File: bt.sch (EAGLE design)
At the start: 16 parts, among them IC1 BLUETOOTH-RN42 HID, Q1 MOSFET-NCHANNELSMD, Q2 MOSFET-NCHANNELSMD

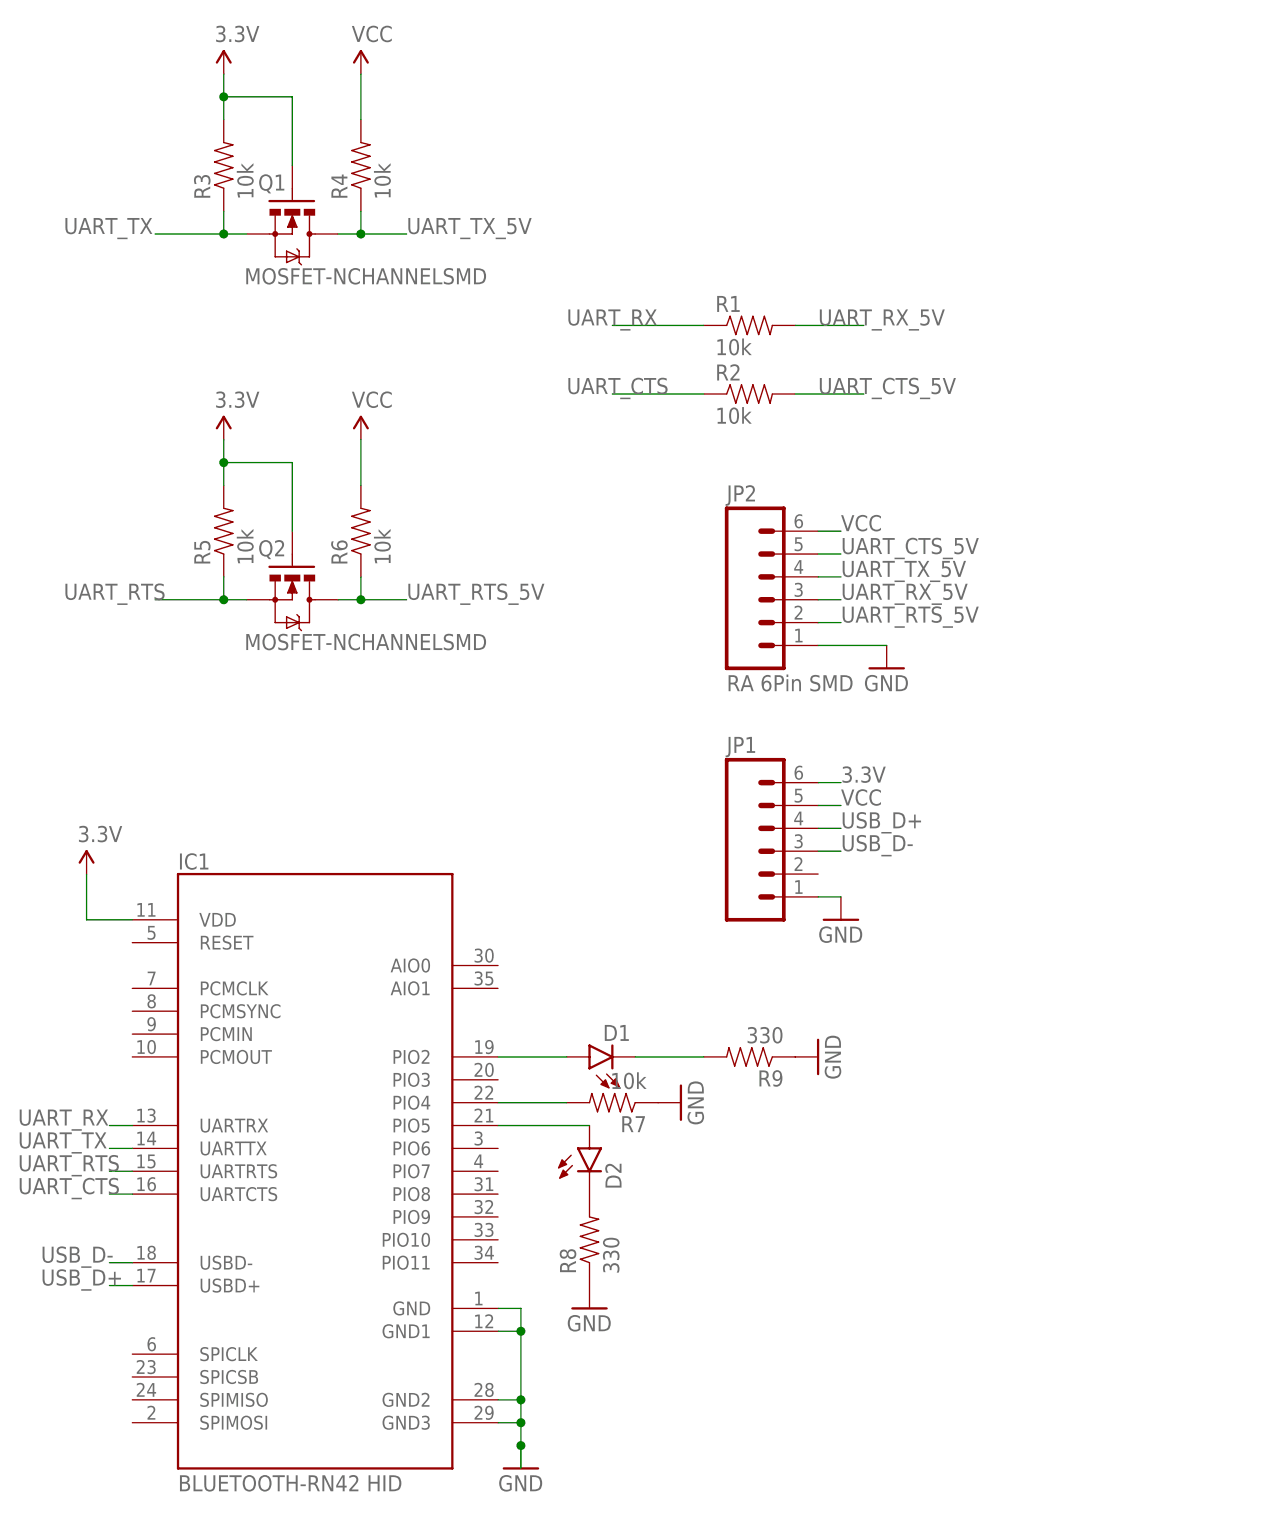
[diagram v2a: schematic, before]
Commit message: Removed silk from bt module and renamed headers
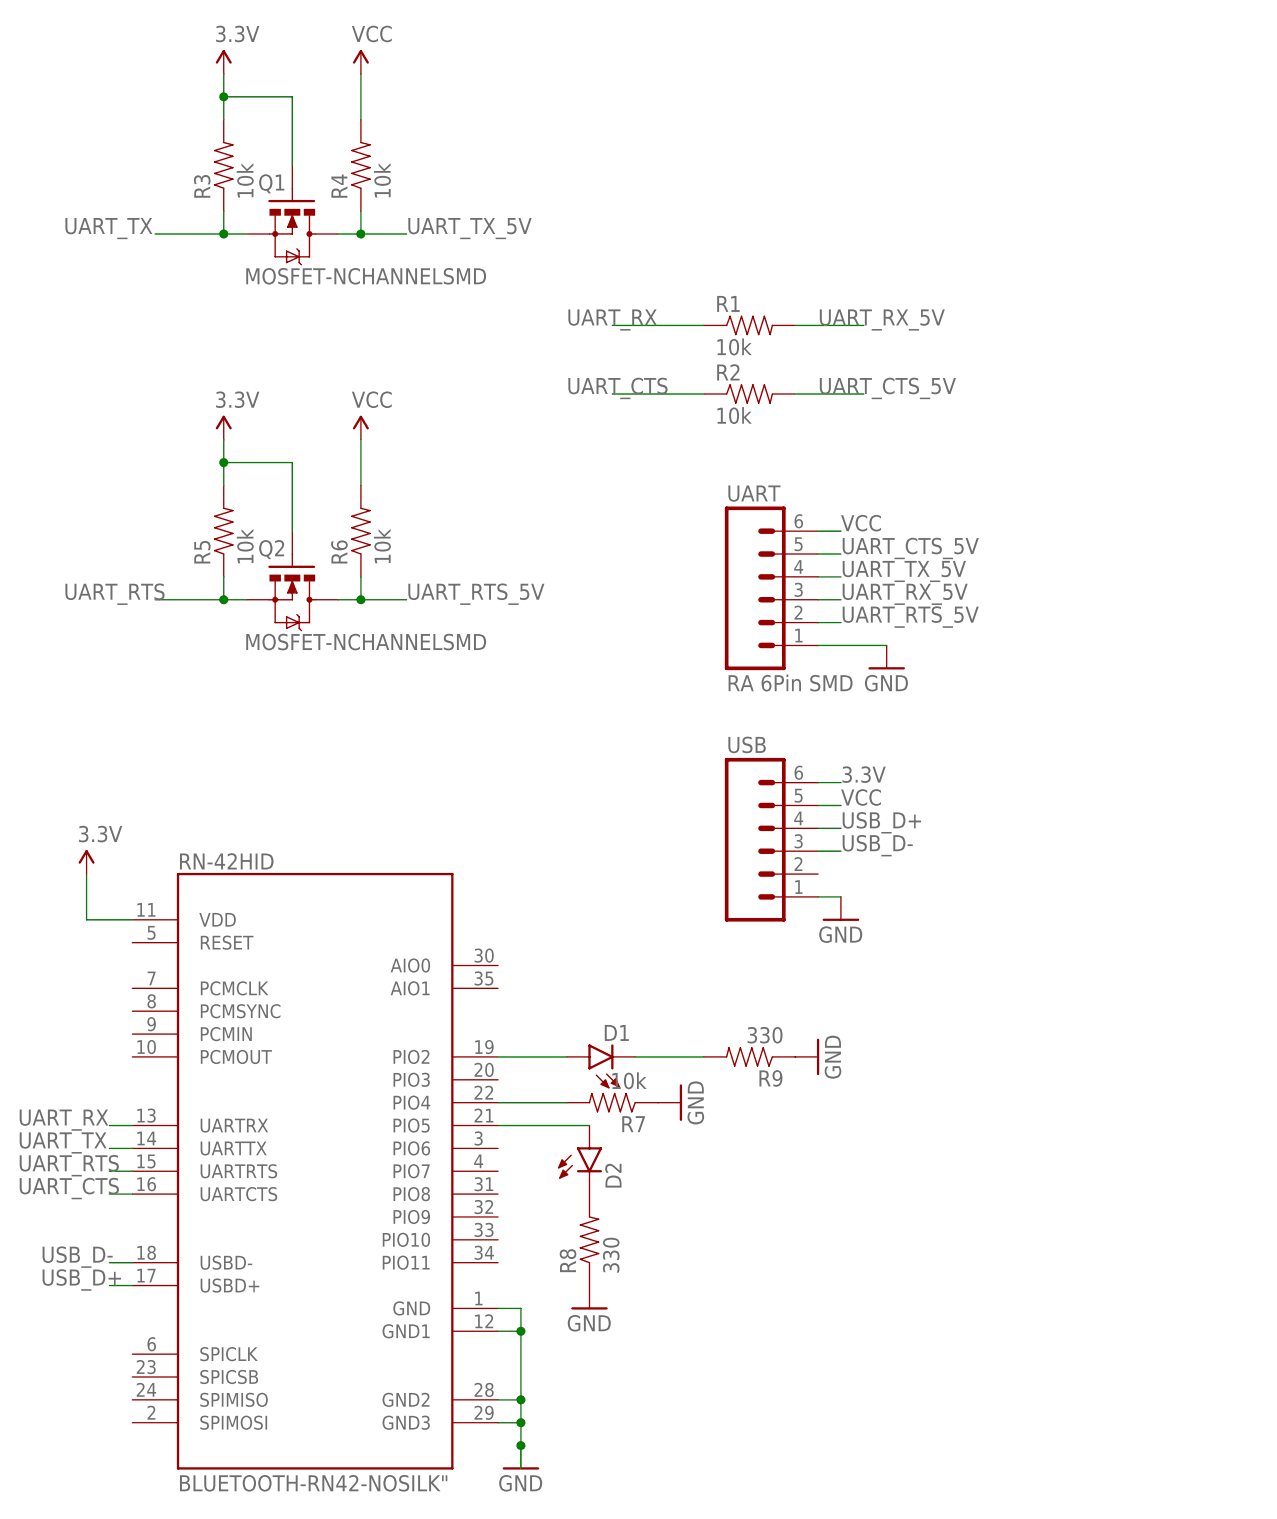
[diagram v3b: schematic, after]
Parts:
- removed IC1: BLUETOOTH-RN42 HID, SparkFun-RF:BLUETOOTH-RN41"
- added RN-42HID: BLUETOOTH-RN42-NOSILK", mine:BLUETOOTH-RN42-NOSILK"
- renumbered JP1 to USB, JP2 to UART
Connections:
- net GND: now also RN-42HID.GND, RN-42HID.GND1, RN-42HID.GND2, RN-42HID.GND3; no longer IC1.GND, IC1.GND1, IC1.GND2, IC1.GND3
- net N$10: now also RN-42HID.PIO5; no longer IC1.PIO5
- net N$8: now also RN-42HID.PIO2; no longer IC1.PIO2
- net N$9: now also RN-42HID.PIO4; no longer IC1.PIO4
- net UART_CTS: now also RN-42HID.UARTCTS; no longer IC1.UARTCTS
- net UART_RTS: now also RN-42HID.UARTRTS; no longer IC1.UARTRTS
- net UART_RX: now also RN-42HID.UARTRX; no longer IC1.UARTRX
- net UART_TX: now also RN-42HID.UARTTX; no longer IC1.UARTTX
- net USB_D+: now also RN-42HID.USBD+; no longer IC1.USBD+
- net USB_D-: now also RN-42HID.USBD-; no longer IC1.USBD-
- net VCC: now also RN-42HID.VDD; no longer IC1.VDD
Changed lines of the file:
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@@
 </classes>
 <parts>
-<part name="IC1" library="SparkFun-RF" deviceset="BLUETOOTH-RN41" device="&quot;" value="BLUETOOTH-RN42 HID"/>
 <part name="Q2" library="SparkFun" deviceset="MOSFET-NCHANNEL" device="SMD"/>
 <part name="P+7" library="SparkFun" deviceset="VCC" device="" value="3.3V"/>
@@
 <part name="GND5" library="SparkFun" deviceset="GND" device=""/>
 <part name="GND6" library="SparkFun" deviceset="GND" device=""/>
-<part name="JP2" library="mine" deviceset="M06" device="SMD-NOHOLES" value="RA 6Pin SMD"/>
-<part name="JP1" library="mine" deviceset="M06" device="SMD-FEMALE-V2-NOSILK"/>
+<part name="UART" library="mine" deviceset="M06" device="SMD-NOHOLES" value="RA 6Pin SMD"/>
+<part name="USB" library="mine" deviceset="M06" device="SMD-FEMALE-V2-NOSILK"/>
+<part name="RN-42HID" library="mine" deviceset="BLUETOOTH-RN42-NOSILK" device="&quot;"/>
 </parts>
 <sheets>
@@
 </plain>
 <instances>
-<instance part="IC1" gate="G$1" x="27.94" y="35.56"/>
 <instance part="Q2" gate="G$1" x="25.4" y="99.06" smashed="yes" rot="R270">
 <attribute name="NAME" x="21.59" y="103.886" size="1.778" layer="95"/>
@@
 <instance part="GND5" gate="1" x="83.82" y="48.26" rot="R90"/>
 <instance part="GND6" gate="1" x="58.42" y="20.32"/>
-<instance part="JP2" gate="G$1" x="78.74" y="99.06"/>
-<instance part="JP1" gate="G$1" x="78.74" y="71.12"/>
+<instance part="UART" gate="G$1" x="78.74" y="99.06"/>
+<instance part="USB" gate="G$1" x="78.74" y="71.12"/>
+<instance part="RN-42HID" gate="G$1" x="27.94" y="35.56"/>
 </instances>
 <busses>
@@
 </segment>
 <segment>
-<pinref part="IC1" gate="G$1" pin="UARTTX"/>
 <wire x1="7.62" y1="38.1" x2="5.08" y2="38.1" width="0.1524" layer="91"/>
 <label x="-5.08" y="38.1" size="1.778" layer="95"/>
+<pinref part="RN-42HID" gate="G$1" pin="UARTTX"/>
 </segment>
 </net>
@@
 <wire x1="83.82" y1="78.74" x2="86.36" y2="78.74" width="0.1524" layer="91"/>
 <label x="86.36" y="78.74" size="1.778" layer="95"/>
-<pinref part="JP1" gate="G$1" pin="6"/>
+<pinref part="USB" gate="G$1" pin="6"/>
 </segment>
 </net>
@@
 <wire x1="83.82" y1="101.6" x2="86.36" y2="101.6" width="0.1524" layer="91"/>
 <label x="86.36" y="101.6" size="1.778" layer="95"/>
-<pinref part="JP2" gate="G$1" pin="4"/>
+<pinref part="UART" gate="G$1" pin="4"/>
 </segment>
 </net>
@@
 </segment>
 <segment>
-<pinref part="IC1" gate="G$1" pin="UARTRX"/>
 <wire x1="7.62" y1="40.64" x2="5.08" y2="40.64" width="0.1524" layer="91"/>
 <label x="-5.08" y="40.64" size="1.778" layer="95"/>
+<pinref part="RN-42HID" gate="G$1" pin="UARTRX"/>
 </segment>
 </net>
@@
 <wire x1="83.82" y1="99.06" x2="86.36" y2="99.06" width="0.1524" layer="91"/>
 <label x="86.36" y="99.06" size="1.778" layer="95"/>
-<pinref part="JP2" gate="G$1" pin="3"/>
+<pinref part="UART" gate="G$1" pin="3"/>
 </segment>
 </net>
@@
 </segment>
 <segment>
-<pinref part="IC1" gate="G$1" pin="VDD"/>
 <wire x1="7.62" y1="63.5" x2="2.54" y2="63.5" width="0.1524" layer="91"/>
 <wire x1="2.54" y1="63.5" x2="2.54" y2="68.58" width="0.1524" layer="91"/>
 <pinref part="P+2" gate="1" pin="VCC"/>
+<pinref part="RN-42HID" gate="G$1" pin="VDD"/>
 </segment>
 <segment>
 <wire x1="83.82" y1="76.2" x2="86.36" y2="76.2" width="0.1524" layer="91"/>
 <label x="86.36" y="76.2" size="1.778" layer="95"/>
-<pinref part="JP1" gate="G$1" pin="5"/>
+<pinref part="USB" gate="G$1" pin="5"/>
 </segment>
 <segment>
 <wire x1="83.82" y1="106.68" x2="86.36" y2="106.68" width="0.1524" layer="91"/>
 <label x="86.36" y="106.68" size="1.778" layer="95"/>
-<pinref part="JP2" gate="G$1" pin="6"/>
+<pinref part="UART" gate="G$1" pin="6"/>
 </segment>
 </net>
@@
 </segment>
 <segment>
-<pinref part="IC1" gate="G$1" pin="UARTRTS"/>
 <wire x1="7.62" y1="35.56" x2="5.08" y2="35.56" width="0.1524" layer="91"/>
 <label x="-5.08" y="35.56" size="1.778" layer="95"/>
+<pinref part="RN-42HID" gate="G$1" pin="UARTRTS"/>
 </segment>
 </net>
@@
 <wire x1="83.82" y1="96.52" x2="86.36" y2="96.52" width="0.1524" layer="91"/>
 <label x="86.36" y="96.52" size="1.778" layer="95"/>
-<pinref part="JP2" gate="G$1" pin="2"/>
+<pinref part="UART" gate="G$1" pin="2"/>
 </segment>
 </net>
@@
 </segment>
 <segment>
-<pinref part="IC1" gate="G$1" pin="UARTCTS"/>
 <wire x1="7.62" y1="33.02" x2="5.08" y2="33.02" width="0.1524" layer="91"/>
 <label x="-5.08" y="33.02" size="1.778" layer="95"/>
+<pinref part="RN-42HID" gate="G$1" pin="UARTCTS"/>
 </segment>
 </net>
@@
 <wire x1="83.82" y1="104.14" x2="86.36" y2="104.14" width="0.1524" layer="91"/>
 <label x="86.36" y="104.14" size="1.778" layer="95"/>
-<pinref part="JP2" gate="G$1" pin="5"/>
+<pinref part="UART" gate="G$1" pin="5"/>
 </segment>
 </net>
 <net name="USB_D-" class="0">
 <segment>
-<pinref part="IC1" gate="G$1" pin="USBD-"/>
 <wire x1="7.62" y1="25.4" x2="5.08" y2="25.4" width="0.1524" layer="91"/>
 <label x="-2.54" y="25.4" size="1.778" layer="95"/>
+<pinref part="RN-42HID" gate="G$1" pin="USBD-"/>
 </segment>
 <segment>
 <wire x1="83.82" y1="71.12" x2="86.36" y2="71.12" width="0.1524" layer="91"/>
 <label x="86.36" y="71.12" size="1.778" layer="95"/>
-<pinref part="JP1" gate="G$1" pin="3"/>
+<pinref part="USB" gate="G$1" pin="3"/>
 </segment>
 </net>
 <net name="USB_D+" class="0">
 <segment>
-<pinref part="IC1" gate="G$1" pin="USBD+"/>
 <wire x1="7.62" y1="22.86" x2="5.08" y2="22.86" width="0.1524" layer="91"/>
 <label x="-2.54" y="22.86" size="1.778" layer="95"/>
+<pinref part="RN-42HID" gate="G$1" pin="USBD+"/>
 </segment>
 <segment>
 <wire x1="83.82" y1="73.66" x2="86.36" y2="73.66" width="0.1524" layer="91"/>
 <label x="86.36" y="73.66" size="1.778" layer="95"/>
-<pinref part="JP1" gate="G$1" pin="4"/>
+<pinref part="USB" gate="G$1" pin="4"/>
 </segment>
 </net>
 <net name="N$8" class="0">
 <segment>
-<pinref part="IC1" gate="G$1" pin="PIO2"/>
 <wire x1="48.26" y1="48.26" x2="55.88" y2="48.26" width="0.1524" layer="91"/>
 <pinref part="D1" gate="G$1" pin="A"/>
+<pinref part="RN-42HID" gate="G$1" pin="PIO2"/>
 </segment>
 </net>
 <net name="N$9" class="0">
 <segment>
-<pinref part="IC1" gate="G$1" pin="PIO4"/>
 <wire x1="48.26" y1="43.18" x2="55.88" y2="43.18" width="0.1524" layer="91"/>
 <pinref part="R7" gate="G$1" pin="2"/>
+<pinref part="RN-42HID" gate="G$1" pin="PIO4"/>
 </segment>
 </net>
 <net name="N$10" class="0">
 <segment>
-<pinref part="IC1" gate="G$1" pin="PIO5"/>
 <wire x1="48.26" y1="40.64" x2="58.42" y2="40.64" width="0.1524" layer="91"/>
 <pinref part="D2" gate="G$1" pin="A"/>
+<pinref part="RN-42HID" gate="G$1" pin="PIO5"/>
 </segment>
 </net>
 <net name="GND" class="0">
 <segment>
-<pinref part="IC1" gate="G$1" pin="GND"/>
 <wire x1="48.26" y1="20.32" x2="50.8" y2="20.32" width="0.1524" layer="91"/>
 <wire x1="50.8" y1="20.32" x2="50.8" y2="17.78" width="0.1524" layer="91"/>
@@
 <junction x="50.8" y="7.62"/>
 <wire x1="50.8" y1="7.62" x2="50.8" y2="5.08" width="0.1524" layer="91"/>
-<pinref part="IC1" gate="G$1" pin="GND1"/>
 <wire x1="50.8" y1="5.08" x2="50.8" y2="2.54" width="0.1524" layer="91"/>
 <wire x1="48.26" y1="17.78" x2="50.8" y2="17.78" width="0.1524" layer="91"/>
-<pinref part="IC1" gate="G$1" pin="GND2"/>
 <wire x1="48.26" y1="10.16" x2="50.8" y2="10.16" width="0.1524" layer="91"/>
-<pinref part="IC1" gate="G$1" pin="GND3"/>
 <wire x1="48.26" y1="7.62" x2="50.8" y2="7.62" width="0.1524" layer="91"/>
 <pinref part="GND3" gate="1" pin="GND"/>
 <junction x="50.8" y="5.08"/>
+<pinref part="RN-42HID" gate="G$1" pin="GND"/>
+<pinref part="RN-42HID" gate="G$1" pin="GND1"/>
+<pinref part="RN-42HID" gate="G$1" pin="GND2"/>
+<pinref part="RN-42HID" gate="G$1" pin="GND3"/>
 </segment>
 <segment>
 <wire x1="83.82" y1="66.04" x2="86.36" y2="66.04" width="0.1524" layer="91"/>
 <pinref part="GND1" gate="1" pin="GND"/>
-<pinref part="JP1" gate="G$1" pin="1"/>
+<pinref part="USB" gate="G$1" pin="1"/>
 </segment>
 <segment>
 <wire x1="83.82" y1="93.98" x2="91.44" y2="93.98" width="0.1524" layer="91"/>
 <pinref part="GND2" gate="1" pin="GND"/>
-<pinref part="JP2" gate="G$1" pin="1"/>
-</segment>
-<segment>
+<pinref part="UART" gate="G$1" pin="1"/>
+</segment>
+<segment>

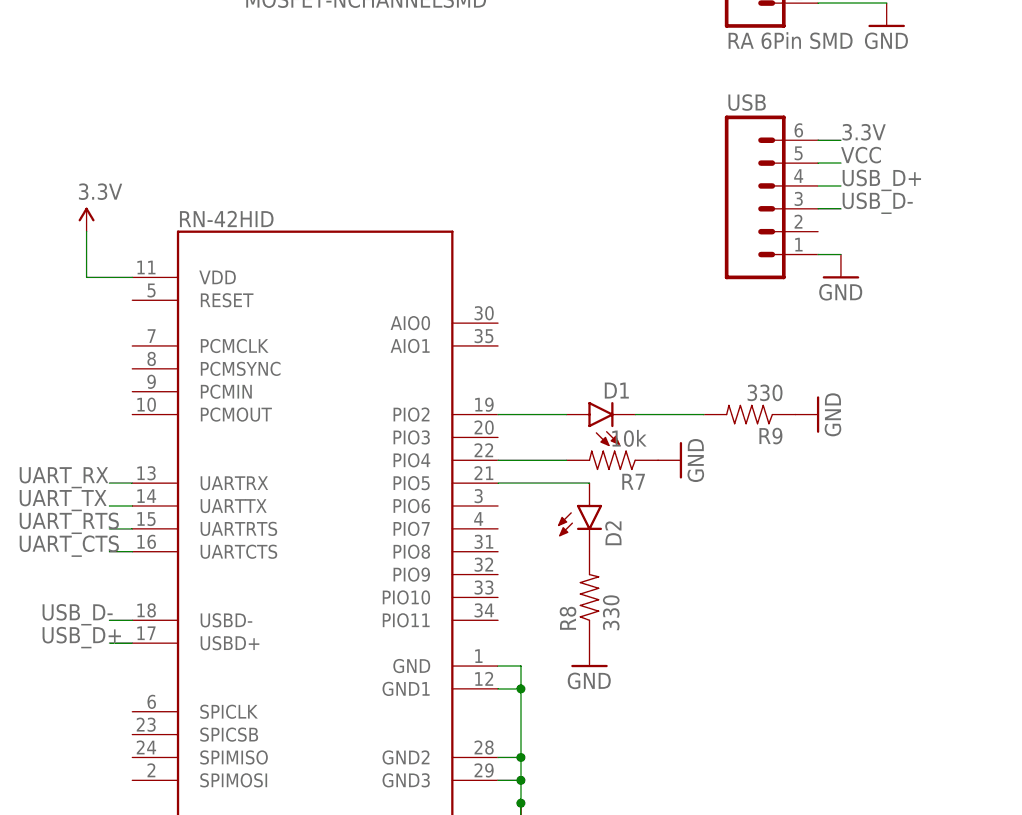
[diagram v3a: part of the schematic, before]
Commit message: Changing which pins are the USB data pins to match the standard
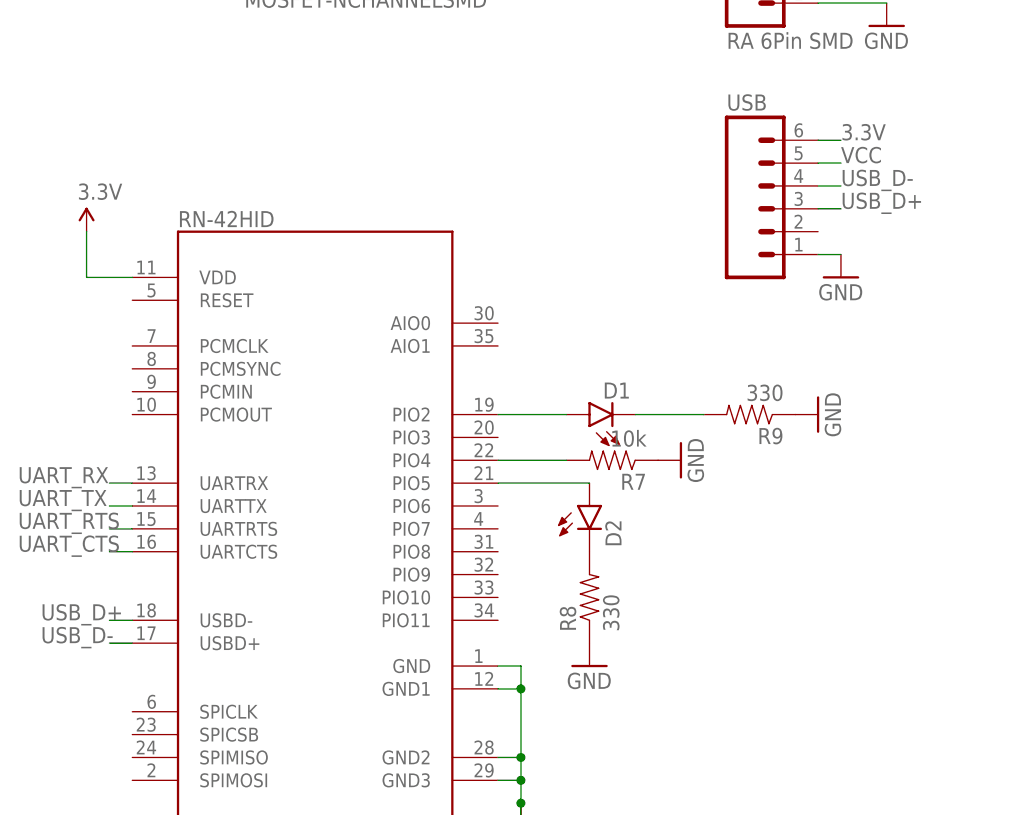
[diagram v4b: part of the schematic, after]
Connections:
- net USB_D+: now also RN-42HID.USBD-, USB.3; no longer RN-42HID.USBD+, USB.4
- net USB_D-: now also RN-42HID.USBD+, USB.4; no longer RN-42HID.USBD-, USB.3
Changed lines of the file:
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@@
 </segment>
 </net>
-<net name="USB_D-" class="0">
+<net name="USB_D+" class="0">
 <segment>
 <wire x1="7.62" y1="25.4" x2="5.08" y2="25.4" width="0.1524" layer="91"/>
@@
 </segment>
 </net>
-<net name="USB_D+" class="0">
+<net name="USB_D-" class="0">
 <segment>
 <wire x1="7.62" y1="22.86" x2="5.08" y2="22.86" width="0.1524" layer="91"/>
